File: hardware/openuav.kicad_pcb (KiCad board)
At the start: 4 copper layers, 36 x 36 mm, 66 parts, among them J1 Conn_01x01, J10 Conn_01x01, J11 Conn_01x01, J12 Conn_01x01, J13 Conn_01x01, J14 Conn_01x01, J19 Conn_01x01, J2 Conn_01x01, J20 Conn_01x01, J22 Conn_01x01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

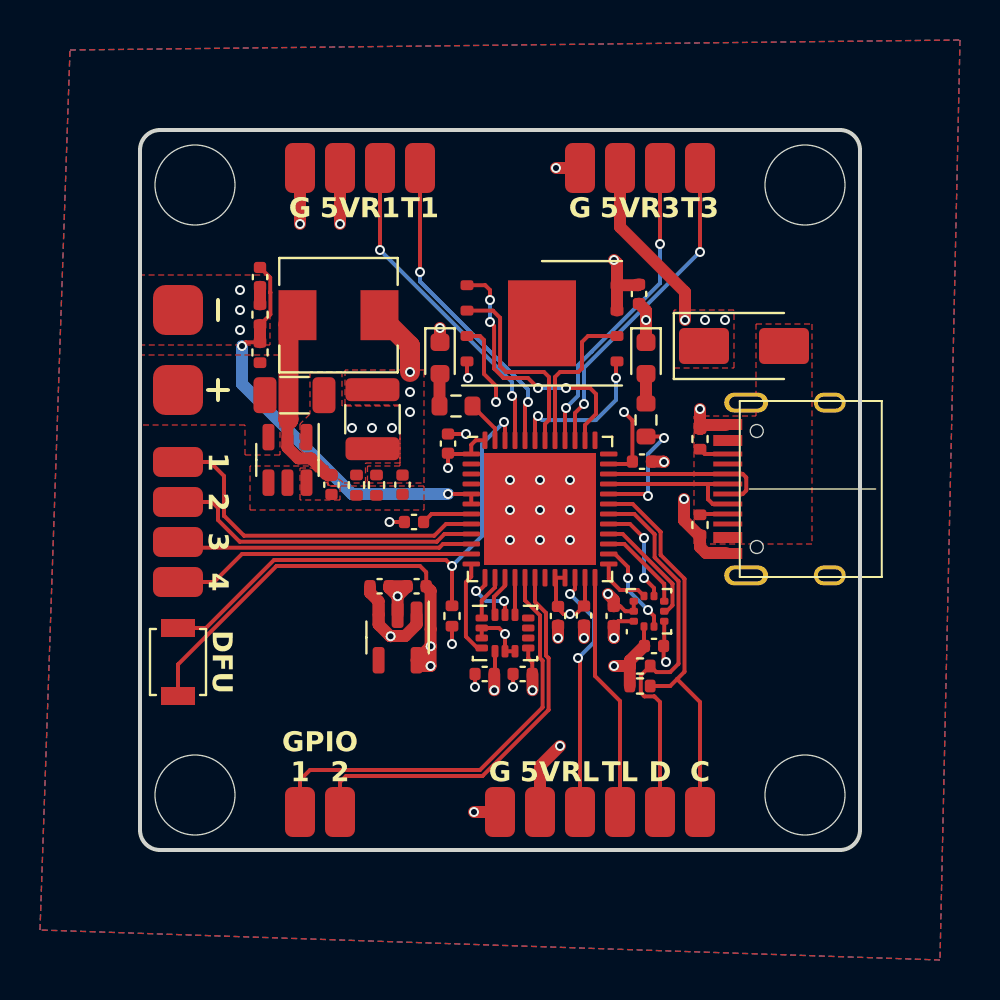
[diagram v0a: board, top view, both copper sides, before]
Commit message: Swap USB power diode for smaller part
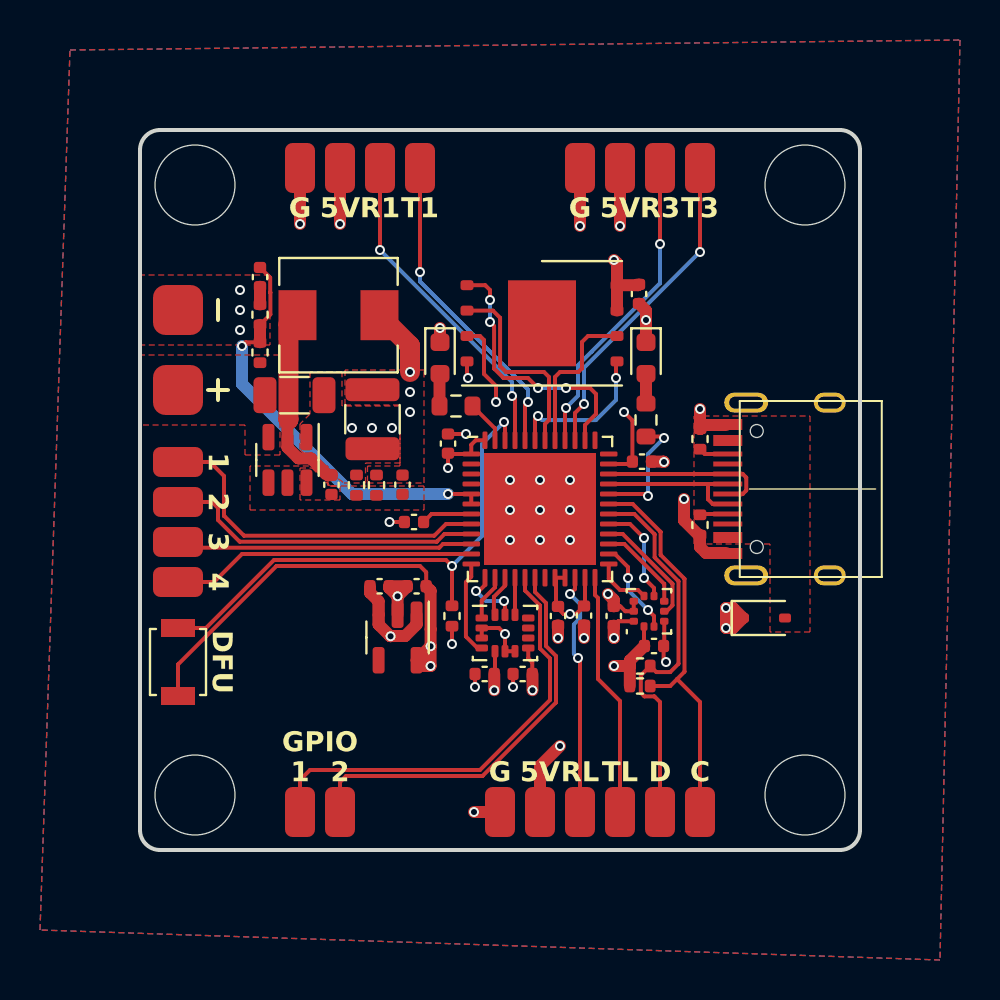
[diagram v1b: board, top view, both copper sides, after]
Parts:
- D1: value SS34 -> PMEG2020AEA; footprint Diode_SMD:D_SMA -> Diode_SMD:D_SOD-323
- moved D1 13.6 mm to (161.2, 74.4)
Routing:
- net +5V: track 23.9 -> 21.8 mm
- net GND: track 33.2 -> 34.9 mm

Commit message: Finish v3 board design
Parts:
- removed J30, J31: Conn_01x01, footprints:largepad
- added C17: 10u, Capacitor_SMD:C_0603_1608Metric, F.Cu at (138.5, 75.2)
- added C18: 10u, Capacitor_SMD:C_0603_1608Metric, F.Cu at (157.6, 78.1)
- added C19: 10u, Capacitor_SMD:C_0603_1608Metric, F.Cu at (152.0, 78.0)
- added C20: 10u, Capacitor_SMD:C_0603_1608Metric, F.Cu at (161.2, 76.7)
- added C21: 10u, Capacitor_SMD:C_0603_1608Metric, F.Cu at (139.2, 56.0)
- added C22: 10u, Capacitor_SMD:C_0603_1608Metric, F.Cu at (141.1, 72.7)
- added C23: 10u, Capacitor_SMD:C_0603_1608Metric, F.Cu at (148.3, 79.7)
- added C8: 10u, Capacitor_SMD:C_0603_1608Metric, F.Cu at (144.1, 75.2)
- added J15: Conn_01x01, footprints:smallpad, F.Cu at (131.9, 60.5)
- added J16: Conn_01x01, footprints:smallpad, F.Cu at (131.9, 58.0)
- added J17: Conn_01x01, footprints:smallpad, F.Cu at (158.0, 84.1)
- added J18: Conn_01x01, footprints:smallpad, F.Cu at (155.5, 84.1)
- added J21: Conn_01x01, footprints:smallpad, F.Cu at (131.9, 73.0)
- added R5: 10k, Resistor_SMD:R_0402_1005Metric, F.Cu at (136.1, 71.6)
- added U5: TLV75733PDBV, Package_TO_SOT_SMD:SOT-23-5, F.Cu at (154.8, 78.1)
- C24, C25: value 1u -> 10u; footprint Capacitor_SMD:C_0402_1005Metric -> Capacitor_SMD:C_0603_1608Metric
- moved J19 32.3 mm to (158.0, 51.9), turned to -90 degrees
- moved J20 32.3 mm to (156.0, 51.9), turned to -90 degrees
- moved R10 20.3 mm to (157.8, 57.7)
- moved R9 20.3 mm to (157.8, 56.7)
- moved D2 18.7 mm to (163.7, 61.1), turned to 180 degrees
- moved C24 15.5 mm to (145.8, 57.4), turned to 90 degrees
- moved R7 15.0 mm to (160.6, 61.1), turned to 0 degrees
- moved C14 13.9 mm to (144.1, 68.6), turned to 90 degrees
- moved J14 13.0 mm to (153.0, 84.1)
- moved J13 12.5 mm to (150.5, 84.1)
- moved C10 11.3 mm to (137.0, 58.3), turned to -90 degrees
- moved R6 11.1 mm to (144.1, 66.8), turned to -90 degrees
- moved R3 10.2 mm to (138.3, 58.2), turned to 90 degrees
- moved J9 10.0 mm to (138.0, 84.1)
- moved R4 9.64 mm to (139.3, 58.2), turned to -90 degrees
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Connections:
- C25 pad 1: +5V -> +3V3
- C3 pad 1: +3V3 -> VDDA
- J10 pad 1: +5V -> +BATT
- U1 pad 32: LED2 -> unconnected-(U1-PA10-Pad32)
- U1 pad 36: SWDIO -> LED1
- U1 pad 37: SWCLK -> LED2
- U1 pad 38: SPI3_CS -> unconnected-(U1-PA15-Pad38)
- U1 pad 47: LED1 -> SPI3_CS
- U1 pad 5: VOLTAGE -> CSENSE
- U3 pad 8: +3V3 -> VDDA
- U7 pad 4: unconnected-(U7-NC-Pad4) -> GND
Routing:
- net +BATT: track 0.00 -> 27.5 mm, vias 0 -> 13
- net GND: track 34.9 -> 60.9 mm, vias 35 -> 51
- net VOLTAGE: track 21.3 -> 7.87 mm, vias 2 -> 0
- net CSENSE: track 0.00 -> 13.4 mm, vias 0 -> 2
- net PWM_5: track 22.4 -> 11.8 mm, vias 0 -> 2
- net UART_4_RX: track 12.3 -> 20.3 mm
- net PWM_6: track 20.6 -> 12.6 mm, vias 0 -> 2
- net LED1: track 2.18 -> 9.63 mm, vias 0 -> 2
- net UART_4_TX: track 12.2 -> 18.2 mm, vias 0 -> 2
- net +3V3: track 52.8 -> 47.5 mm, vias 11 -> 13
- net VDDA: track 0.00 -> 5.33 mm
- net SPI3_CS: track 13.4 -> 8.79 mm, vias 4 -> 2
- net CURRENT: track 0.00 -> 4.27 mm
- net LED2: track 6.17 -> 10.1 mm
- net PWM_1: track 17.6 -> 21.0 mm
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- added copper zone on In1.Cu, net +BATT
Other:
- board text added: "-B+"
- board text added: "CK"
- board text added: "CS"
- board text added: "DA"
- board text added: "OPENUAV v0.3"
- board text added: "RV"
- board text added: "S1"
- board text added: "S2"
- board text added: "TV"
- board text removed: "C"
- board text removed: "D"
- board text removed: "GPIO"
- board text removed: "OPENUAV v0.2"
- board text removed: "RL"
- board text removed: "TL"

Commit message: Rework supply rail capacitors
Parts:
- added C26: 1u, Capacitor_SMD:C_0402_1005Metric, F.Cu at (150.2, 78.2)
- C25: value 10u -> 1u; footprint Capacitor_SMD:C_0603_1608Metric -> Capacitor_SMD:C_0402_1005Metric
- moved C25 15.7 mm to (146.9, 64.2), turned to 0 degrees
- moved C23 0.30 mm to (148.0, 79.7)
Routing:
- net GND: track 60.9 -> 70.6 mm
- net SPI1_INT: track 4.77 -> 5.93 mm, vias 0 -> 2
- net +3V3: track 47.5 -> 46.8 mm, vias 13 -> 14
